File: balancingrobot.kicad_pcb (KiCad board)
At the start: 2 copper layers, 95 x 82 mm, 56 parts, among them J1 Conn_01x04, J10 Conn_01x02, J11 Conn_01x02, J12 Conn_01x02, J13 Conn_01x02, J2 Conn_01x06, J3 Conn_01x06, J4 Conn_01x02, J5 Conn_01x22, J6 Conn_01x22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

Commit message: Update silkscreen and change to 4 layer
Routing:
- net +3V3: track 382.1 -> 151.2 mm, vias 3 -> 6
- net /IR_R: track 64.4 -> 62.7 mm, vias 2 -> 0
- net GND: track 82.1 -> 81.5 mm
- net /IR_L: vias 2 -> 0
- net /DSP_DAT: vias 4 -> 3
- added copper zone on In1.Cu, net +3V3
- added copper zone on In2.Cu, net GND
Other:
- copper layers 2 -> 4
- board text added: "16299 Balancing Robot Rev 1 - March 2025 Carson Swoveland"
- board text added: "A0/M2A"
- board text added: "A1/M2B"
- board text added: "L Encoder (HV!)"
- board text added: "MOTOR 1"
- board text added: "MOTOR 2"
- board text added: "R Encoder (HV!)"
- board text added: "VBSENSE"
- board text removed: "L Encoder (HV)"
- board text removed: "R Encoder (HV)"

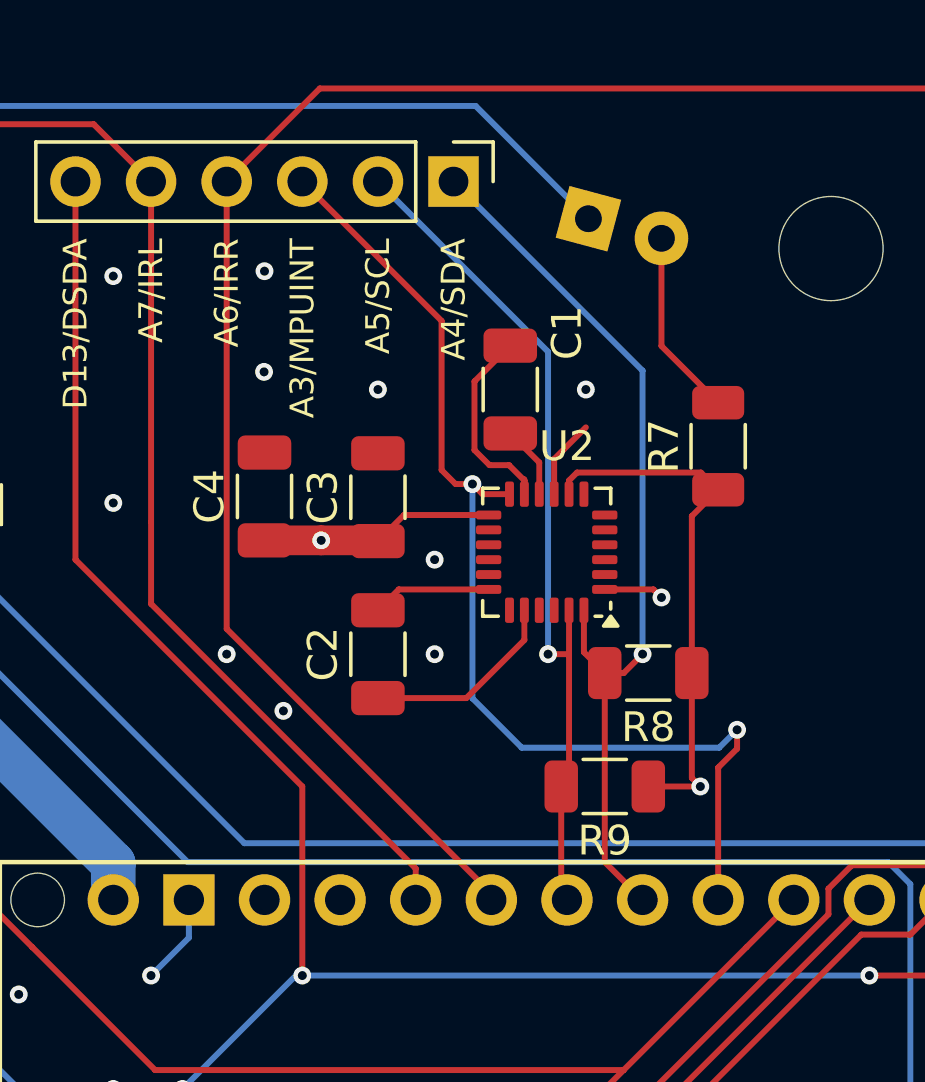
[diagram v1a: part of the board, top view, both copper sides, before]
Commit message: Remove MPU6050
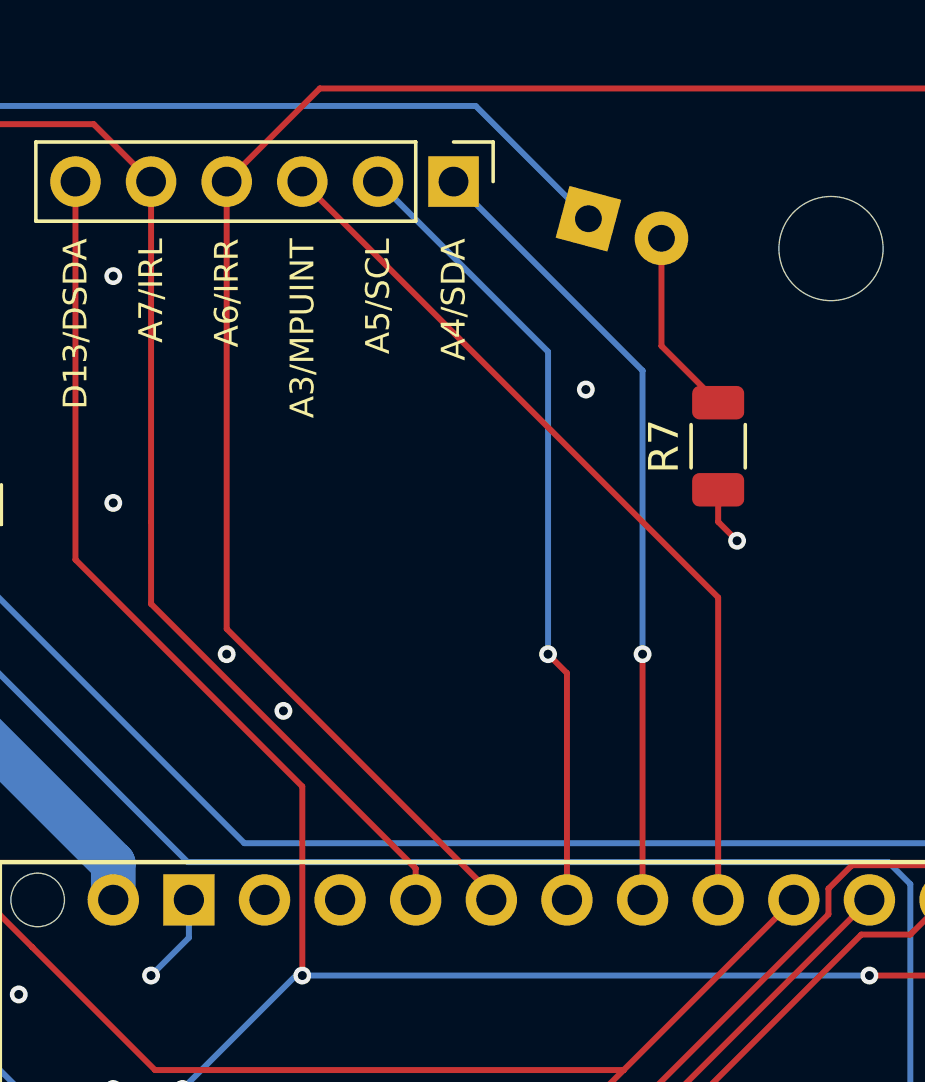
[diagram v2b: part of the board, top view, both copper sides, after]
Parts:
- removed C1, C4: 0.1uF, Capacitor_SMD:C_1206_3216Metric
- removed C2: 2.2nF, Capacitor_SMD:C_1206_3216Metric
- removed C3: 10nF, Capacitor_SMD:C_1206_3216Metric
- removed R8, R9: 4.7k, Resistor_SMD:R_1206_3216Metric
- removed U2: MPU-6050, Sensor_Motion:InvenSense_QFN-24_4x4mm_P0.5mm
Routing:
- net +3V3: track 151.2 -> 127.3 mm, vias 6 -> 5
- net GND: track 81.5 -> 65.7 mm, vias 41 -> 35
- net /MPU_INT: track 37.2 -> 29.9 mm, vias 2 -> 0
- net Net-(U2-CPOUT): track 6.73 -> 0.00 mm
- net /SDA: track 30.6 -> 26.8 mm
- net Net-(U2-REGOUT): track 2.44 -> 0.00 mm
- net /SCL: track 28.9 -> 27.0 mm

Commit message: Update readme
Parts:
- added G***: LOGO, Custom:salix, F.Cu at (108.0, 61.6)
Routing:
- net GND: track 65.7 -> 68.4 mm, vias 35 -> 50
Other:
- board text added: "+3V3"
- board text added: "16299 Balancing Robot Rev 2 - May 2025 Carson Swoveland"
- board text added: "JLCJLCJLCJLC"
- board text added: "↑ USB"
- board text removed: "16299 Balancing Robot Rev 1 - March 2025 Carson Swoveland"
